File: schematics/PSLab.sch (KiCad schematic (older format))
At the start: 73 parts, among them CON1 USB-MINI-B, J1 Programmer, J10 GND, J11 Vbus, J13 D+, J14 D-, J16 I2C-2, J2 DoublePins, J5 Bluetooth, J6 I2C-1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

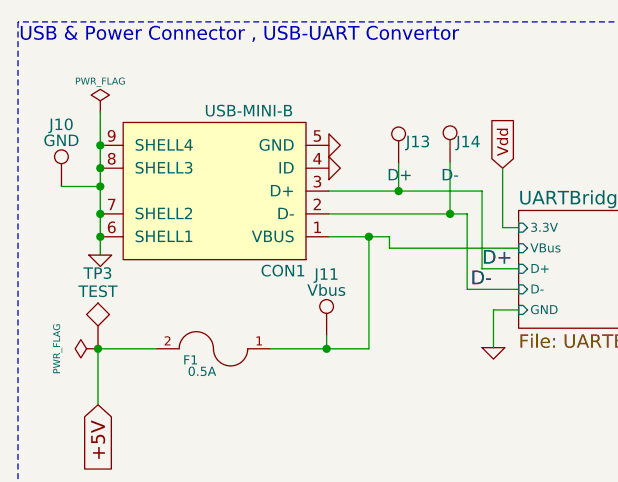
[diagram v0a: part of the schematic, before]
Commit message: feat: usb c port with 12 pins
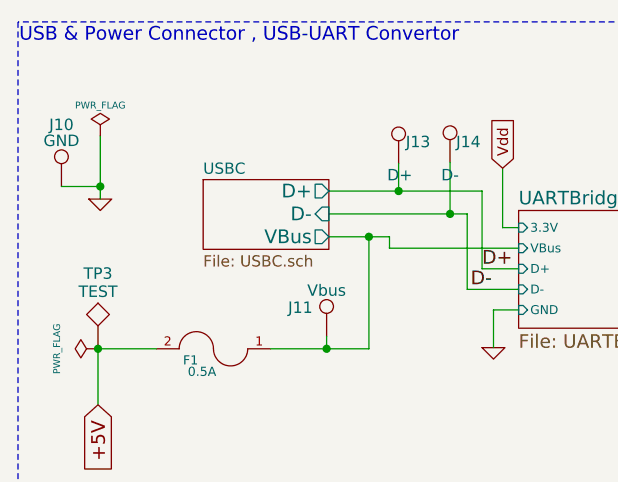
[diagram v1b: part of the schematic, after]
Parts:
- removed CON1: USB-MINI-B, Custom_Components:USB_Micro-B, symbol PSLab-rescue:USB-MINI-B
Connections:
- wire segments 273 -> 267
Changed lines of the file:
@@
 $Descr A4 11693 8268
 encoding utf-8
-Sheet 1 5
+Sheet 1 6
 Title "PSLab"
 Date "2019-03-03"
@@
 L power:PWR_FLAG #FLG010
 U 1 1 54C819ED
-P 860 895
-F 0 "#FLG010" H 860 990 30  0001 C CNN
-F 1 "PWR_FLAG" H 860 1030 30  0000 C CNN
-F 2 "" H 860 895 60  0000 C CNN
-F 3 "" H 860 895 60  0000 C CNN
-	1    860  895
+P 860 1000
+F 0 "#FLG010" H 860 1095 30  0001 C CNN
+F 1 "PWR_FLAG" H 860 1135 30  0000 C CNN
+F 2 "" H 860 1000 60  0000 C CNN
+F 3 "" H 860 1000 60  0000 C CNN
+	1    860  1000
 	1    0    0    -1
 $EndComp
@@
 L PSLab-rescue:GND-RESCUE-proto1 #PWR023
 U 1 1 556DA4CB
-P 860 1520
-F 0 "#PWR023" H 860 1520 30  0001 C CNN
-F 1 "GND" H 860 1450 30  0001 C CNN
-F 2 "" H 860 1520 60  0000 C CNN
-F 3 "" H 860 1520 60  0000 C CNN
-	1    860  1520
-	1    0    0    -1
-$EndComp
-$Comp
-L PSLab-rescue:GND-RESCUE-proto1 #PWR024
-U 1 1 556DA5BD
-P 1860 1040
-F 0 "#PWR024" H 1860 1040 30  0001 C CNN
-F 1 "GND" H 1860 970 30  0001 C CNN
-F 2 "" H 1860 1040 60  0000 C CNN
-F 3 "" H 1860 1040 60  0000 C CNN
-	1    1860 1040
-	0    -1   -1   0
+P 860 1275
+F 0 "#PWR023" H 860 1275 30  0001 C CNN
+F 1 "GND" H 860 1205 30  0001 C CNN
+F 2 "" H 860 1275 60  0000 C CNN
+F 3 "" H 860 1275 60  0000 C CNN
+	1    860  1275
+	1    0    0    -1
 $EndComp
 $Comp
@@
 Mounting Holes
 $Comp
-L PSLab-rescue:GND-RESCUE-proto1 #PWR037
-U 1 1 556DA7E3
-P 1860 1140
-F 0 "#PWR037" H 1860 1140 30  0001 C CNN
-F 1 "GND" H 1860 1070 30  0001 C CNN
-F 2 "" H 1860 1140 60  0000 C CNN
-F 3 "" H 1860 1140 60  0000 C CNN
-	1    1860 1140
-	0    -1   -1   0
-$EndComp
-$Comp
 L PSLab-rescue:MMBT3904 Q2
 U 1 1 5A319DE9
@@
 $EndComp
 $Comp
-L PSLab-rescue:USB-MINI-B CON1
-U 1 1 5A6CB48C
-P 1360 1240
-F 0 "CON1" H 1060 1590 50  0000 C CNN
-F 1 "USB-MINI-B" H 1210 890 50  0000 C CNN
-F 2 "Custom_Components:USB_Micro-B" H 1360 1140 50  0001 C CNN
-F 3 "" H 1360 1140 50  0000 C CNN
-	1    1360 1240
-	-1   0    0    1
-$EndComp
-$Comp
 L PSLab-rescue:TEST_1P J13
 U 1 1 5A6F40E4
@@
 U 1 1 5A6F5463
 P 1850 1875
-F 0 "J11" H 1850 2145 50  0000 C CNN
+F 0 "J11" H 1735 2000 50  0000 C CNN
 F 1 "Vbus" H 1850 2075 50  0000 C CNN
 F 2 "Measurement_Points:Measurement_Point_Square-SMD-Pad_Small" H 2050 1875 50  0001 C CNN
@@
 	1860 1340 2390 1340
 Wire Wire Line
-	860  1340 865  1340
-Wire Wire Line
-	865  1140 860  1140
-Wire Wire Line
 	1605 1930 1850 1930
 Wire Wire Line
@@
 	4605 815  4545 815
 Wire Wire Line
-	860  895  860  1040
-Connection ~ 860  1440
-Connection ~ 860  1340
-Connection ~ 860  1140
-Wire Wire Line
 	7050 3250 7050 3100
 Wire Wire Line
 	690  1220 860  1220
-Connection ~ 860  1220
 Wire Wire Line
 	1850 1875 1850 1930
@@
 	2475 3450 2475 3750
 Wire Wire Line
-	860  1440 860  1520
-Wire Wire Line
-	860  1340 860  1440
-Wire Wire Line
-	860  1140 860  1220
-Wire Wire Line
-	860  1220 860  1340
-Wire Wire Line
 	1850 1930 2035 1930
 Wire Wire Line
@@
 	-1   0    0    1
 $EndComp
-Connection ~ 860  1040
-Wire Wire Line
-	860  1040 860  1140
 Wire Wire Line
 	3400 4400 3400 5300
@@
 Wire Wire Line
 	8750 1475 8750 1775
+$Sheet
+S 1310 1190 550  305
+U 5ED254D7
+F0 "USBC" 49
+F1 "USBC.sch" 49
+F2 "VBus" O R 1860 1440 60
+F3 "D+" O R 1860 1240 60
+F4 "D-" I R 1860 1340 60
+$EndSheet
+Wire Wire Line
+	860  1000 860  1220
+Wire Wire Line
+	860  1220 860  1275
+Connection ~ 860  1220
 $EndSCHEMATC

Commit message: feat: external power circuit schematics
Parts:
- removed J7: UART/ESP, Pin_Headers:Pin_Header_Straight_1x07_Pitch2.54mm, symbol PSLab-rescue:Conn_01x07
- removed TP3: TEST, Measurement_Points:Measurement_Point_Round-SMD-Pad_Small, symbol PSLab-rescue:TEST
- removed TP5, TP6, TP7: Fiducial, Fiducials:Fiducial_0.5mm_Dia_1mm_Outer, symbol PSLab-rescue:TEST
- added C3: 10u, Capacitor_SMD:C_0603_1608Metric, symbol Device:C
- added C5: 1u, Capacitor_SMD:C_0603_1608Metric, symbol Device:C
- added F2: 2016L100PR(1A), Fuse:Fuse_1206_3216Metric, symbol Device:Fuse
- added J15: External Power, Connector_PinSocket_2.54mm:PinSocket_1x03_P2.54mm_Vertical, symbol Connector_Generic:Conn_01x03
- added J7: UART/ESP, Connector_PinSocket_2.54mm:PinSocket_1x06_P2.54mm_Vertical, symbol Connector_Generic:Conn_01x06
- added SW1: Power Route, Button_Switch_THT:SW_CuK_JS202011CQN_DPDT_Straight, symbol Switch:SW_Push_DPDT
- added TP5, TP6, TP7: Fiducial, Fiducial:Fiducial_0.5mm_Mask1mm, symbol PSLab:Logos
- added U18: LDL212PU50R, Package_DFN_QFN:DFN-6-1EP_3x3mm_P0.95mm_EP1.7x2.6mm, symbol PSLab:LDL212PU50R
- C10, C13, C15, C17, C2, C20, C21, C4, C8, C9: footprint Capacitors_SMD:C_0603 -> Capacitor_SMD:C_0603_1608Metric
- D1, D2: footprint Diodes_SMD:D_MiniMELF -> Diode_SMD:D_MiniMELF
- D3, D4: footprint LEDs:LED_0805 -> LED_SMD:LED_0805_2012Metric
- F1: footprint Fuse_Holders_and_Fuses:Fuse_SMD1206_Reflow -> Fuse:Fuse_1206_3216Metric
- J1: footprint Pin_Headers:Pin_Header_Straight_1x06_Pitch2.54mm -> Connector_PinSocket_2.54mm:PinSocket_1x05_P2.54mm_Vertical; symbol PSLab-rescue:Conn_01x06 -> Connector_Generic:Conn_01x05
- J10, J11, J13, J14: footprint Measurement_Points:Measurement_Point_Square-SMD-Pad_Small -> TestPoint:TestPoint_Pad_1.0x1.0mm
- R1, R10, R11, R12, R13, R2, R3, R4, R49, R5, R52, R53, R54, R55, R56, R57, R6, R7, R8, R9: footprint Resistors_SMD:R_0603 -> Resistor_SMD:R_0603_1608Metric
- TP4: footprint Measurement_Points:Measurement_Point_Round-SMD-Pad_Small -> TestPoint:TestPoint_Pad_1.0x1.0mm
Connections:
- net labels added: ExP, InP
- net labels removed: SW
- wire segments 267 -> 290
- no-connect marks 13 -> 11
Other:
- note added: "External Power"
- moved on the sheet: C2, U15

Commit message: feat: UART resets
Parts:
- removed JP1: ESP Reset, Connectors:GS2, symbol Jumper:SolderJumper_2_Bridged
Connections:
- wire segments 290 -> 288
- no-connect marks 11 -> 12
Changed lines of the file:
@@
 Wire Wire Line
 	1765 6030 1765 6120
-$Comp
-L Jumper:SolderJumper_2_Bridged JP1
-U 1 1 5C990A98
-P 8145 1175
-F 0 "JP1" H 8265 1285 50  0000 C CNN
-F 1 "ESP Reset" H 8025 1280 39  0000 C CNN
-F 2 "Connectors:GS2" H 8145 1175 50  0001 C CNN
-F 3 "~" H 8145 1175 50  0001 C CNN
-	1    8145 1175
-	0    1    1    0
-$EndComp
-$Comp
-L PSLab-rescue:GND-RESCUE-proto1 #PWR08
-U 1 1 5C9910C8
-P 8145 1025
-F 0 "#PWR08" H 8145 1025 30  0001 C CNN
-F 1 "GND" H 8145 955 30  0001 C CNN
-F 2 "" H 8145 1025 60  0000 C CNN
-F 3 "" H 8145 1025 60  0000 C CNN
-	1    8145 1025
-	-1   0    0    1
-$EndComp
 Wire Wire Line
 	3400 4400 3400 5300
@@
 Wire Wire Line
 	8395 1275 8395 1475
-Wire Wire Line
-	8145 1375 8470 1375
-Wire Wire Line
-	8145 1325 8145 1375
 Wire Wire Line
 	9170 1375 9420 1375
@@
 $EndComp
 NoConn ~ 5050 2600
+NoConn ~ 8470 1375
 $EndSCHEMATC

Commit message: enhancement: improve routing
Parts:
- J7: footprint Connector_PinSocket_2.54mm:PinSocket_1x06_P2.54mm_Vertical -> Connector_PinSocket_2.54mm:PinSocket_1x05_P2.54mm_Vertical; symbol Connector_Generic:Conn_01x06 -> Connector_Generic:Conn_01x05
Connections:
- net +5V: now also J7.1 (Pin_1); no longer J7.5 (Pin_5)
- net Vdd: now also J7.5 (Pin_5); no longer J7.6 (Pin_6)
- net ESPROG: no longer names the net of U15.6 (RST)
- net ESPROG: no longer J7.1 (Pin_1)
- no-connect marks 12 -> 13
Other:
- note added: "WiFi"
- note removed: "For WiFi Option"
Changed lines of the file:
@@
 	1    0    0    -1
 $EndComp
-Text Notes 8785 2140 0    60   ~ 0
-For WiFi Option
+Text Notes 9300 2140 0    60   ~ 0
+WiFi
 Text Notes 505  595  0    60   ~ 0
 USB & Power Connector , USB-UART Convertor
@@
 	0    -1   -1   0
 $EndComp
-Text Label 7485 1685 0    60   ~ 0
-ESPROG
 $Comp
 L PSLab-rescue:CONN_1 MH2
@@
 	-1   0    0    1
 $EndComp
-Text GLabel 6775 1895 1    40   Input ~ 0
+Text GLabel 7175 1895 1    40   Input ~ 0
 +5V
 Text GLabel 1415 3550 0    40   Input ~ 0
@@
 Text GLabel 1000 7080 2    40   Input ~ 0
 RxD
-Text GLabel 6675 1895 1    47   Input ~ 0
+Text GLabel 6775 1895 1    47   Input ~ 0
 Vdd
 $Sheet
@@
 Wire Wire Line
 	6775 850  6975 850
-Wire Wire Line
-	9420 2025 8210 2025
 Wire Notes Line
 	500  2750 4075 2750
@@
 Wire Wire Line
 	8175 5940 8375 5940
-Wire Wire Line
-	7175 1685 8210 1685
 Wire Notes Line
 	500  500  500  2750
@@
 Connection ~ 2475 3450
 Wire Wire Line
-	8210 1685 8210 2025
-Wire Wire Line
 	9870 4135 9870 4400
 Wire Wire Line
@@
 	7145 1495 7075 1495
 Connection ~ 7075 1495
-Wire Wire Line
-	7175 1685 7175 1895
 Wire Notes Line
 	1255 6680 1255 7735
@@
 Wire Wire Line
 	8395 1275 8395 1475
-Wire Wire Line
-	9170 1375 9420 1375
-Wire Wire Line
-	9420 1375 9420 2025
 Connection ~ 8395 1475
 NoConn ~ 9170 1275
@@
 ExP
 $Comp
-L Connector_Generic:Conn_01x06 J7
+L Connector_Generic:Conn_01x05 J7
 U 1 1 5EF3BE2C
 P 6975 2095
 F 0 "J7" V 6975 2370 50  0000 L CNN
 F 1 "UART/ESP" V 7085 1855 50  0000 L CNN
-F 2 "Connector_PinSocket_2.54mm:PinSocket_1x06_P2.54mm_Vertical" H 6975 2095 50  0001 C CNN
+F 2 "Connector_PinSocket_2.54mm:PinSocket_1x05_P2.54mm_Vertical" H 6975 2095 50  0001 C CNN
 F 3 "~" H 6975 2095 50  0001 C CNN
 	1    6975 2095
@@
 NoConn ~ 5050 2600
 NoConn ~ 8470 1375
+NoConn ~ 9170 1375
 $EndSCHEMATC

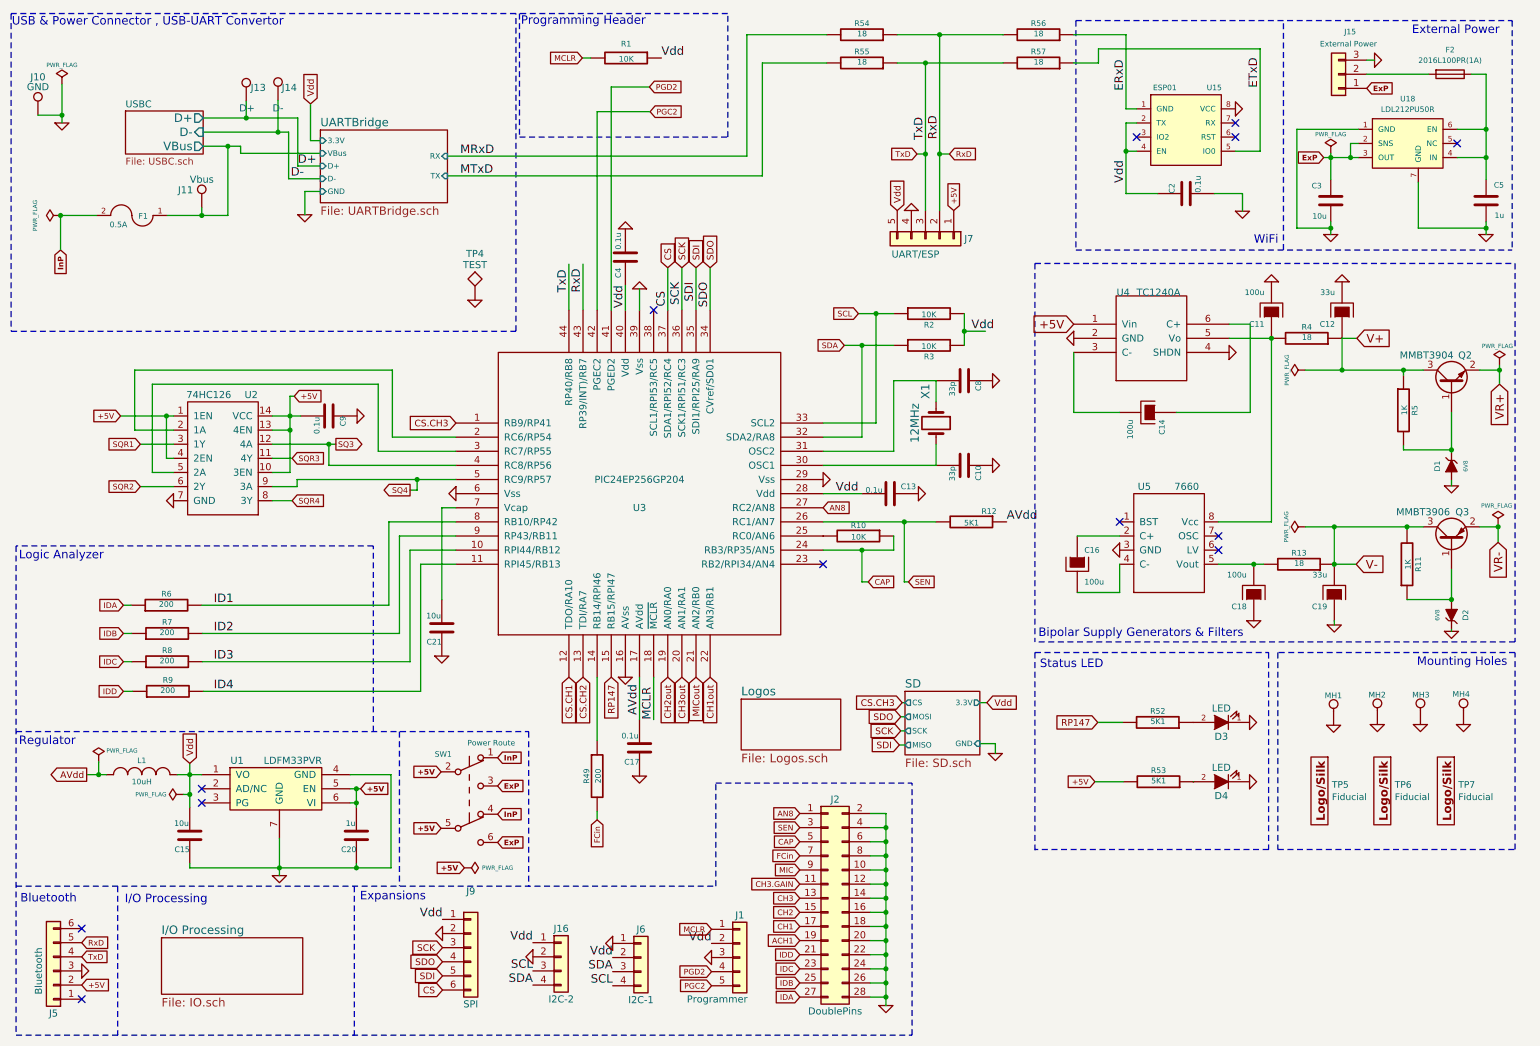
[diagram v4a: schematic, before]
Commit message: feat: dual UART support
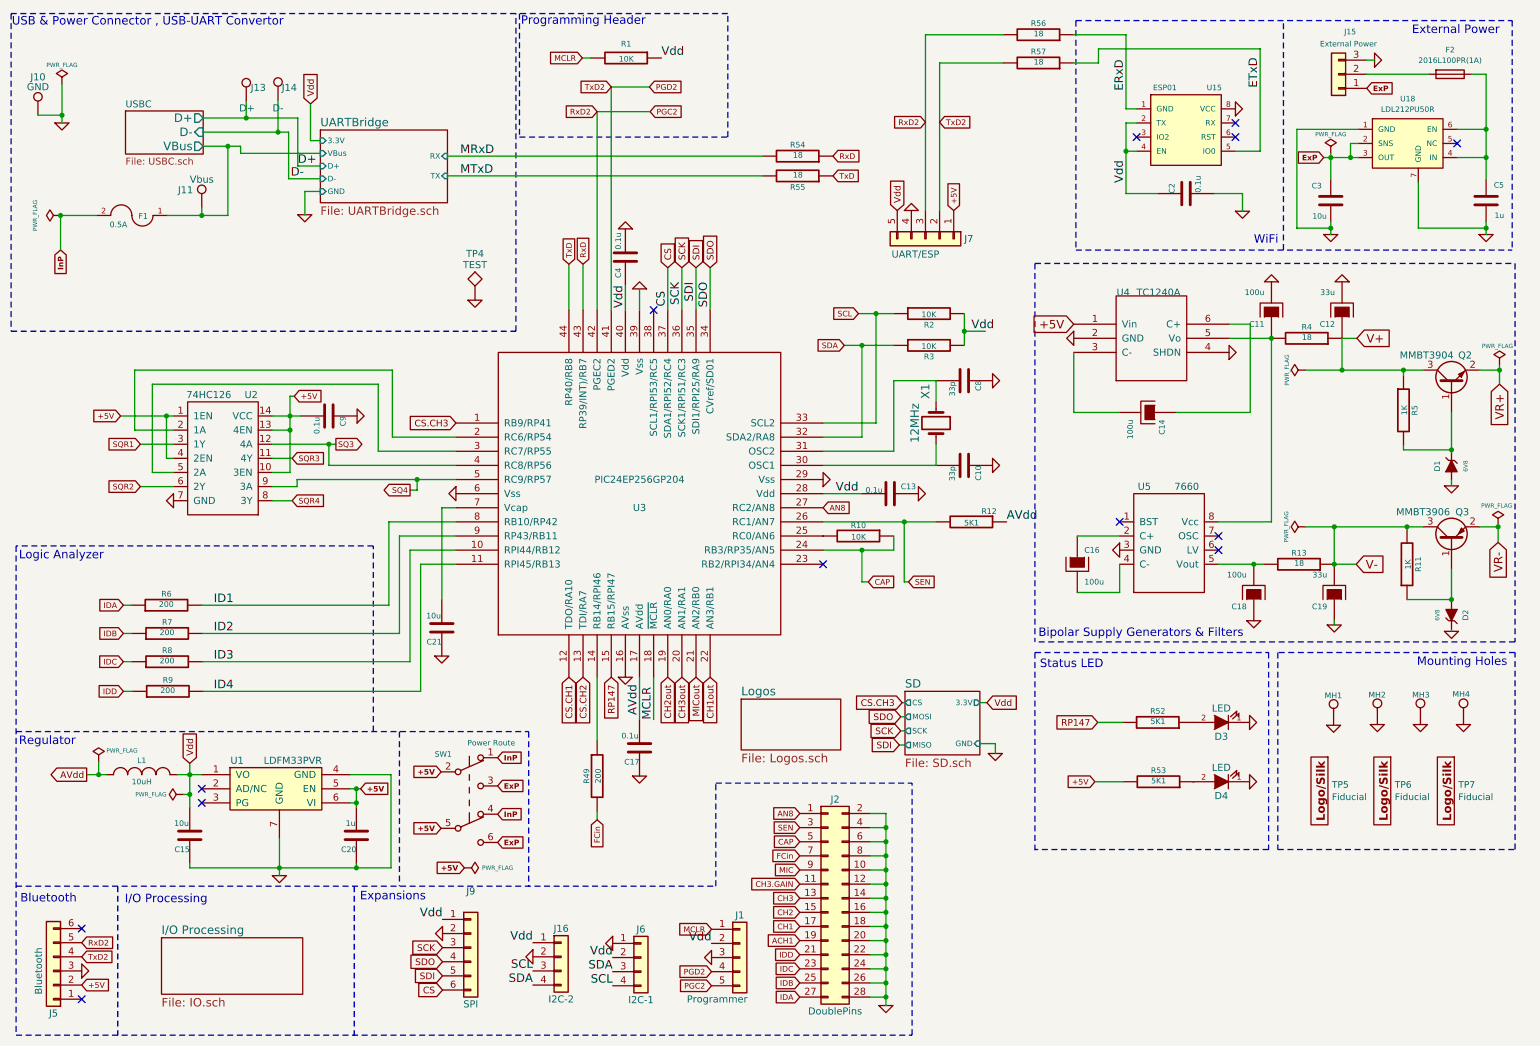
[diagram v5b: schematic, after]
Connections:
- net PGC2: now also J5.5 (Pin_5), J7.3 (Pin_3), R56.2
- net PGD2: now also J5.4 (Pin_4), J7.2 (Pin_2), R57.2
- net RxD: no longer J5.5 (Pin_5), J7.2 (Pin_2), R56.2
- net TxD: no longer J5.4 (Pin_4), J7.3 (Pin_3), R57.2
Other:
- moved on the sheet: R54, R55
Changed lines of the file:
@@
 Text Label 8395 825  3    60   ~ 0
 ERxD
-Text Label 4550 2475 1    60   ~ 0
-RxD
-Text Label 4450 2475 1    60   ~ 0
-TxD
 Text GLabel 6085 6665 0    40   Input ~ 0
 CH3.GAIN
@@
 Text GLabel 1035 5890 0    47   Output ~ 0
 AVdd
-Text Label 7075 1390 1    60   ~ 0
-RxD
-Text Label 6975 1395 1    60   ~ 0
-TxD
 Text GLabel 3325 3875 0    40   Output ~ 0
 SQ4
@@
 +5V
 $Comp
-L PSLab-rescue:R-RESCUE-proto1 R55
-U 1 1 566549A7
-P 6525 850
-F 0 "R55" V 6605 850 40  0000 C CNN
-F 1 "18" V 6532 851 40  0000 C CNN
-F 2 "Resistor_SMD:R_0603_1608Metric" V 6455 850 30  0001 C CNN
-F 3 "" H 6525 850 30  0000 C CNN
-	1    6525 850
-	0    1    -1   0
-$EndComp
-$Comp
 L PSLab-rescue:R-RESCUE-proto1 R57
 U 1 1 56654C7F
@@
 F 3 "" H 7775 850 30  0000 C CNN
 	1    7775 850
-	0    1    -1   0
-$EndComp
-$Comp
-L PSLab-rescue:R-RESCUE-proto1 R54
-U 1 1 56655363
-P 6525 650
-F 0 "R54" V 6605 650 40  0000 C CNN
-F 1 "18" V 6532 651 40  0000 C CNN
-F 2 "Resistor_SMD:R_0603_1608Metric" V 6455 650 30  0001 C CNN
-F 3 "" H 6525 650 30  0000 C CNN
-	1    6525 650
 	0    1    -1   0
 $EndComp
@@
 NoConn ~ 1000 7480
 NoConn ~ 1000 6980
-Text GLabel 6915 1495 0    40   Input ~ 0
+Text GLabel 6320 1650 2    40   Input ~ 0
 TxD
-Text GLabel 7145 1495 2    40   Input ~ 0
+Text GLabel 6320 1510 2    40   Input ~ 0
 RxD
 Text GLabel 1000 7380 2    40   Input ~ 0
@@
 $EndComp
 Text GLabel 1000 7180 2    40   Input ~ 0
-TxD
+TxD2
 Text GLabel 1000 7080 2    40   Input ~ 0
-RxD
+RxD2
 Text GLabel 6775 1895 1    47   Input ~ 0
 Vdd
@@
 Wire Wire Line
 	8200 850  8025 850
-Wire Wire Line
-	6775 650  7075 650
-Wire Wire Line
-	6775 850  6975 850
 Wire Notes Line
 	500  2750 4075 2750
@@
 	6880 7735 6880 5950
 Wire Wire Line
-	6975 850  6975 1495
-Connection ~ 6975 850
-Wire Wire Line
-	7075 650  7075 1495
-Connection ~ 7075 650
-Wire Wire Line
 	1650 3550 1415 3550
 Wire Wire Line
@@
 Wire Notes Line
 	3065 4270 535  4270
-Wire Wire Line
-	6915 1495 6975 1495
-Connection ~ 6975 1495
-Wire Wire Line
-	7145 1495 7075 1495
-Connection ~ 7075 1495
 Wire Notes Line
 	1255 6680 1255 7735
@@
 	2930 6680 2930 7735
 Wire Wire Line
-	3590 1510 5710 1510
-Wire Wire Line
 	3590 1650 5820 1650
-Wire Wire Line
-	6275 650  5710 650
-Wire Wire Line
-	5710 650  5710 1510
-Wire Wire Line
-	6275 850  5820 850
-Wire Wire Line
-	5820 850  5820 1650
 Wire Wire Line
 	2580 1925 2580 1760
@@
 	1850 1930 2035 1930
 Wire Wire Line
-	6975 850  7525 850
-Wire Wire Line
-	7075 650  7525 650
-Wire Wire Line
 	2750 3550 2800 3550
 Wire Wire Line
@@
 Wire Wire Line
 	6695 7465 6695 7525
-Wire Wire Line
-	6975 1495 6975 1895
-Wire Wire Line
-	7075 1495 7075 1895
 Wire Wire Line
 	2035 1440 2125 1440
@@
 NoConn ~ 8470 1375
 NoConn ~ 9170 1375
+$Comp
+L PSLab-rescue:R-RESCUE-proto1 R55
+U 1 1 566549A7
+P 6070 1650
+F 0 "R55" V 5990 1650 40  0000 C CNN
+F 1 "18" V 6077 1651 40  0000 C CNN
+F 2 "Resistor_SMD:R_0603_1608Metric" V 6000 1650 30  0001 C CNN
+F 3 "" H 6070 1650 30  0000 C CNN
+	1    6070 1650
+	0    1    -1   0
+$EndComp
+$Comp
+L PSLab-rescue:R-RESCUE-proto1 R54
+U 1 1 56655363
+P 6070 1510
+F 0 "R54" V 6150 1510 40  0000 C CNN
+F 1 "18" V 6077 1511 40  0000 C CNN
+F 2 "Resistor_SMD:R_0603_1608Metric" V 6000 1510 30  0001 C CNN
+F 3 "" H 6070 1510 30  0000 C CNN
+	1    6070 1510
+	0    1    -1   0
+$EndComp
+Wire Wire Line
+	3590 1510 5820 1510
+Text GLabel 4450 2275 1    40   Input ~ 0
+TxD
+Text GLabel 4550 2275 1    40   Input ~ 0
+RxD
+Text GLabel 6975 1270 0    40   Input ~ 0
+RxD2
+Text GLabel 7075 1270 2    40   Input ~ 0
+TxD2
+Text GLabel 4750 1020 0    40   Input ~ 0
+TxD2
+Text GLabel 4650 1195 0    40   Input ~ 0
+RxD2
+Wire Wire Line
+	6975 650  7525 650
+Wire Wire Line
+	7075 1895 7075 850
+Wire Wire Line
+	7075 850  7525 850
+Wire Wire Line
+	6975 1895 6975 650
 $EndSCHEMATC
